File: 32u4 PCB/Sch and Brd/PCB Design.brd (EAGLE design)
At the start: 95.8 x 64.6 mm, 54 parts, among them J1 AVR_SPI_PROG_3X2PTH, J2 AMP FCI 10103594-0001LF, Q1 16MHz, U1 ATMEGA32U4-AU

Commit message: Started routinng
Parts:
- removed JP1: (no value), pinhead:1X02
- removed USB-ASP: AVR_SPI_PROG_5X2PTH2, SparkFun-Connectors:2X5-SHROUDED
- added I2C_OLED: (no value), pinhead:1X04
- added MPU6040: (no value), pinhead:1X08
- added SPI_SD_CARD: (no value), pinhead:1X06
- added X1: (no value), con-ptr500:AK500/2-H
- moved R12 153.5 mm to (75.7, 32.3), turned to 90 degrees
- moved JP5 145.2 mm to (78.2, -1.78), turned to 90 degrees
- moved JP4 143.4 mm to (76.5, 1.78), turned to 90 degrees
- moved JP3 141.7 mm to (84.8, -2.03), turned to 90 degrees
- moved R11 139.7 mm to (73.2, 31.0), turned to 90 degrees
- moved JP2 137.6 mm to (66.0, 30.0), turned to 90 degrees
- moved BUTTON_2 123.7 mm to (54.6, 0.00), turned to 180 degrees
- moved BUTTON_1 108.9 mm to (68.6, -0.25)
- moved POWER_PORT 105.4 mm to (72.6, 17.8), turned to 90 degrees
- moved C11 97.5 mm to (43.2, 31.8), turned to 180 degrees
- moved PB2 80.5 mm to (33.5, 50.3), turned to 90 degrees
- moved CONT 75.4 mm to (82.3, 12.2), turned to 270 degrees
- moved R10 73.1 mm to (23.4, 20.3), turned to 180 degrees
- moved R8 72.8 mm to (28.4, 49.3), turned to 90 degrees
- moved PB1 70.7 mm to (26.9, 52.1), turned to 90 degrees
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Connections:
- net PD2 renamed PD2/RXD1
- net PD3 renamed PD3/TXD1
- net PF4 renamed PF4/TCK
- net PF5 renamed PF5/TMS
- net PF6 renamed PF6/TDO
- net PF7 renamed PF7/TDI
- removed net PB1: J1.3, PORT_B.3, PORT_B.4, U1.9, USB-ASP.7
- removed net PB2: J1.4, PORT_B.5, PORT_B.6, U1.10, USB-ASP.1
- removed net PB3: J1.1, PORT_B.7, PORT_B.8, U1.11, USB-ASP.9
- removed net PD0: PORT_D.1, PORT_D.2, U1.18
- removed net PD1: PORT_D.3, PORT_D.4, U1.19
- new net AD0: MPU6040.7
- new net CS: SPI_SD_CARD.1
- new net INT: MPU6040.8
- new net PB1/SCK: J1.3, PORT_B.3, PORT_B.4, SPI_SD_CARD.2, U1.9
- new net PB2/MOSI: J1.4, PORT_B.5, PORT_B.6, SPI_SD_CARD.3, U1.10
- new net PB3/MISO: J1.1, PORT_B.7, PORT_B.8, SPI_SD_CARD.4, U1.11
- new net PD0/SCL: I2C_OLED.3, MPU6040.3, PORT_D.1, PORT_D.2, U1.18
- new net PD1/SDA: I2C_OLED.4, MPU6040.4, PORT_D.3, PORT_D.4, U1.19
- new net XCL: MPU6040.6
- new net XDA: MPU6040.5
- net +12V: now also X1.2; no longer JP1.1
- net +5V: now also I2C_OLED.2, MPU6040.1, SPI_SD_CARD.5; no longer USB-ASP.2
- net GND: now also I2C_OLED.1, MPU6040.2, SPI_SD_CARD.6, X1.1; no longer JP1.2, USB-ASP.10, USB-ASP.4, USB-ASP.6, USB-ASP.8
- net RESET: no longer USB-ASP.5
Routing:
- net +5V: track 237.2 -> 6.49 mm, vias 6 -> 0
- net RESET: track 113.9 -> 0.00 mm, vias 1 -> 0
- net 3.3V: track 76.8 -> 0.00 mm, vias 2 -> 0
- net PB3/MISO: track 0.00 -> 59.6 mm, vias 0 -> 4
- net PB2: track 56.6 -> 0.00 mm, vias 2 -> 0
- net +12V: track 55.1 -> 0.00 mm, vias 1 -> 0
- net PB2/MOSI: track 0.00 -> 51.6 mm, vias 0 -> 3
- net PB3: track 49.0 -> 0.00 mm
- net PD2/RXD1: track 20.4 -> 68.0 mm, vias 1 -> 3
- net PB1: track 47.5 -> 0.00 mm
- net PD7: track 0.00 -> 44.4 mm, vias 0 -> 2
- net PD6: track 0.00 -> 44.0 mm, vias 0 -> 2
- net PB5: track 2.55 -> 45.0 mm, vias 0 -> 2
- net PD1/SDA: track 0.00 -> 42.3 mm, vias 0 -> 2
- net PB4: track 2.55 -> 44.6 mm, vias 0 -> 2
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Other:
- board text removed: "3.3V"
- board text removed: "5V"
- board text removed: "AREF"
- board text removed: "CTS"
- board text removed: "DTR"
- board text removed: "PB0"
- board text removed: "PB1"
- board text removed: "PB2"
- board text removed: "PB3"
- board text removed: "PB4"
- board text removed: "PB5"
- board text removed: "PC0"
- board text removed: "PC1"
- board text removed: "PC2"
- board text removed: "PC3"
- board text removed: "PC4"
- board text removed: "PC5"
- board text removed: "PD0"
- board text removed: "PD1"
- board text removed: "PD2"
- board text removed: "PD3"
- board text removed: "PD4"
- board text removed: "PD5"
- board text removed: "PD6"
- board text removed: "PD7"
- board text removed: "RESET"
- board text removed: "RX"
- board text removed: "SCL"
- board text removed: "SDA"
- board text removed: "TX"

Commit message: Started routinng
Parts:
- removed CONT: 50k, pot:S64W
- added I2C: (no value), pinhead:1X04
- added R13: 220, resistor:M0805
- moved J1 70.6 mm to (64.8, 58.9), turned to 180 degrees
- moved C4 61.4 mm to (23.9, 58.7)
- moved R11 58.4 mm to (23.6, 0.00)
- moved R12 57.8 mm to (27.9, -0.25)
- moved JP2 55.7 mm to (18.8, 0.51)
- moved C3 51.4 mm to (43.2, 0.25), turned to 270 degrees
- moved BUTTON_1 45.4 mm to (24.4, 10.2)
- moved JP3 45.3 mm to (39.6, 0.00), turned to 270 degrees
- moved JP4 44.7 mm to (31.8, 0.00)
- moved JP5 42.7 mm to (35.6, 0.00), turned to 270 degrees
- moved BUTTON_2 42.1 mm to (13.7, 10.2), turned to 0 degrees
- moved PB1 38.3 mm to (15.5, 15.5), turned to 0 degrees
- moved PB2 35.9 mm to (24.6, 15.5), turned to 0 degrees
- moved R6 34.0 mm to (17.3, 17.5), turned to 180 degrees
- moved R8 31.8 mm to (26.4, 17.5), turned to 180 degrees
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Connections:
- net +12V: no longer X1.2
- net +5V: now also I2C.2; no longer CONT.E
- net GND: now also I2C.1, R13.1; no longer CONT.A, X1.1
- net N$6: now also R13.2; no longer CONT.S
- net PD0/SCL: now also I2C.3
- net PD1/SDA: now also I2C.4
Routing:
- net N$15: track 0.00 -> 60.8 mm, vias 0 -> 2
- net N$13: track 0.00 -> 60.7 mm, vias 0 -> 2
- net PD0/SCL: track 37.5 -> 66.2 mm, vias 0 -> 2
- net PD1/SDA: track 42.3 -> 70.2 mm, vias 2 -> 4
- net PB4: track 44.6 -> 20.0 mm, vias 2 -> 1
- net PB5: track 45.0 -> 20.7 mm, vias 2 -> 1
- net PB0: track 40.0 -> 17.0 mm, vias 1 -> 0
- net RESET: track 0.00 -> 22.9 mm
- net PB6: track 2.54 -> 22.5 mm, vias 0 -> 1
- net PB1/SCK: track 41.7 -> 51.2 mm, vias 2 -> 1
- net PB3/MISO: track 59.6 -> 53.7 mm, vias 4 -> 2
- net PB2/MOSI: track 51.6 -> 54.6 mm
- net PC7: track 29.3 -> 30.2 mm
- net PD3/TXD1: track 65.4 -> 64.6 mm
- net PC6: track 29.1 -> 29.7 mm
- added copper zone on layer 16, net +5V
- removed copper zone on layer 16, net GND
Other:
- board text removed: "GND"
- board text removed: "Vin"

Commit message: Rough layout ready
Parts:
- POWER: device pinhead:2X03 -> pinhead:2X04
- moved R13 31.6 mm to (77.2, 9.91)
- moved C11 30.3 mm to (66.0, 51.6), turned to 90 degrees
- moved C10 17.3 mm to (62.5, 28.7), turned to 0 degrees
- moved C2 7.41 mm to (54.6, 27.7)
- moved C4 4.07 mm to (23.6, 62.7), turned to 90 degrees
- moved C9 2.05 mm to (24.1, 42.7)
- moved R10 1.70 mm to (19.8, 23.6)
- moved R9 1.61 mm to (19.8, 21.1)
- moved R3 1.27 mm to (20.6, 62.7)
- moved POWER 0.51 mm to (35.3, 9.14)
- moved R2 0.51 mm to (32.5, 57.7)
- moved C7 0.18 mm to (20.2, 33.8), turned to 0 degrees
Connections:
- net +5V: now also POWER.3, POWER.4
- net AREF: no longer POWER.3, POWER.4
- net GND: now also POWER.7, POWER.8
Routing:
- net RESET: track 22.9 -> 103.5 mm, vias 0 -> 1
- net +5V: track 6.49 -> 60.6 mm, vias 0 -> 4
- net PE6: track 0.00 -> 38.7 mm, vias 0 -> 1
- net PD0/SCL: track 66.2 -> 96.1 mm
- net +12V: track 0.00 -> 26.6 mm
- net PD1/SDA: track 70.2 -> 96.3 mm
- net PB7: track 2.54 -> 26.0 mm, vias 0 -> 2
- net N$16: track 0.00 -> 19.2 mm, vias 0 -> 1
- net AREF: track 0.00 -> 17.3 mm, vias 0 -> 1
- net D-: track 0.00 -> 12.2 mm, vias 0 -> 2
- net D+: track 0.00 -> 12.1 mm, vias 0 -> 2
- net 3V3: track 0.00 -> 10.2 mm
- net N$6: track 0.00 -> 7.09 mm
- net 3.3V: track 0.00 -> 7.08 mm
- net N$14: track 0.00 -> 3.43 mm
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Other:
- board size 95.8 x 64.6 mm -> 78 x 64.6 mm

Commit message: Routing almost done
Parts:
- removed JP2, JP3, JP4, JP5: JUMPER-SMT_3_1-NC_PASTE_SILK, SparkFun-Jumpers:SMT-JUMPER_3_1-NC_PASTE_SILK
- removed PB1, PB2, PB5: Yellow, SparkFun-LED:LED-0603
- added PC6, PE2, PE6: Yellow, SparkFun-LED:LED-0603
- LCD1: value LCD-16X2NOSILK -> LCD-16X2NOHOLES; device SparkFun-Displays:LCD-16X2_NOSILK -> SparkFun-Displays:LCD-16X2_NOHOLESNOSILK
- R4, R5, R6, R8: value 1K -> 330
- moved LCD1 73.5 mm to (47.5, -13.2), turned to 0 degrees
- moved J2 66.5 mm to (74.7, 0.76), turned to 270 degrees
- moved R13 58.7 mm to (19.6, -1.27), turned to 0 degrees
- moved R7 56.2 mm to (50.5, 4.83), turned to 0 degrees
- moved R10 53.4 mm to (67.8, 0.25), turned to 0 degrees
- moved R9 51.4 mm to (67.8, 2.79), turned to 0 degrees
- moved I2C 32.5 mm to (42.2, 66.5), turned to 180 degrees
- moved POW 28.4 mm to (39.4, 15.7), turned to 90 degrees
- moved R6 27.8 mm to (45.0, 20.3)
- moved R4 24.3 mm to (45.0, 24.9)
- moved X1 24.2 mm to (11.7, 51.3)
- moved C3 20.9 mm to (31.8, 17.8), turned to 0 degrees
- moved R5 19.3 mm to (31.8, 20.3)
- moved R8 19.2 mm to (45.0, 22.6)
- moved R12 16.2 mm to (31.8, 15.5), turned to 0 degrees
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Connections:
- removed net CS: SPI_SD_CARD.1
- removed net D4: LCD1.11
- removed net D5: LCD1.12
- removed net D6: LCD1.13
- removed net D7: LCD1.14
- removed net E: LCD1.6
- removed net N$10: PB1.A
- removed net N$11: PB2.A
- removed net N$12: PB5.A
- removed net N$17: JP2.2, R11.1
- removed net N$18: BUTTON_1.3, BUTTON_1.4, JP3.2
- removed net N$19: BUTTON_2.3, BUTTON_2.4, JP5.2
- removed net N$20: JP4.2, R12.1
- removed net PB0: PORT_B.1, PORT_B.2, U1.8
- removed net RS: LCD1.4
- new net PB0/SS: PORT_B.1, PORT_B.2, SPI_SD_CARD.1, U1.8
- net +5V: now also R11.1, R12.1; no longer JP2.1, JP3.3, JP4.1, JP5.3
- net GND: now also BUTTON_1.3, BUTTON_1.4, BUTTON_2.3, BUTTON_2.4; no longer JP2.3, JP3.1, JP4.3, JP5.1
- net N$1: now also PC6.C; no longer PB5.C
- net N$3: now also PE6.C; no longer PB1.C
- net N$7: now also PE2.C; no longer PB2.C
- net PC6: now also PC6.A
- net PD0/SCL: now also I2C.4; no longer I2C.3
- net PD1/SDA: now also I2C.3; no longer I2C.4
- net PE2: now also PE2.A
- net PE6: now also PE6.A
- net PF0: now also LCD1.4
- net PF1: now also LCD1.6
- net PF4/TCK: now also LCD1.11
- net PF5/TMS: now also LCD1.12
- net PF6/TDO: now also LCD1.13
- net PF7/TDI: now also LCD1.14
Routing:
- net PIN: track 0.00 -> 61.1 mm, vias 0 -> 2
- net PF0: track 24.8 -> 80.3 mm
- net PF1: track 24.1 -> 70.0 mm
- net N$13: track 61.6 -> 33.4 mm, vias 2 -> 0
- net PF4/TCK: track 23.3 -> 50.1 mm
- net PF5/TMS: track 22.8 -> 48.9 mm
- net PB2/MOSI: track 54.6 -> 29.3 mm, vias 3 -> 4
- net PB1/SCK: track 51.2 -> 26.6 mm
- net PB0/SS: track 0.00 -> 21.9 mm
- net N$15: track 62.6 -> 41.2 mm
- net PB3/MISO: track 53.7 -> 32.7 mm, vias 2 -> 1
- net PF6/TDO: track 23.5 -> 43.5 mm
- net PF7/TDI: track 24.2 -> 42.8 mm
- net PD3/TXD1: track 64.8 -> 82.6 mm, vias 4 -> 2
- net PB0: track 16.6 -> 0.00 mm
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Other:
- board size 78 x 64.6 mm -> 71.6 x 74.8 mm

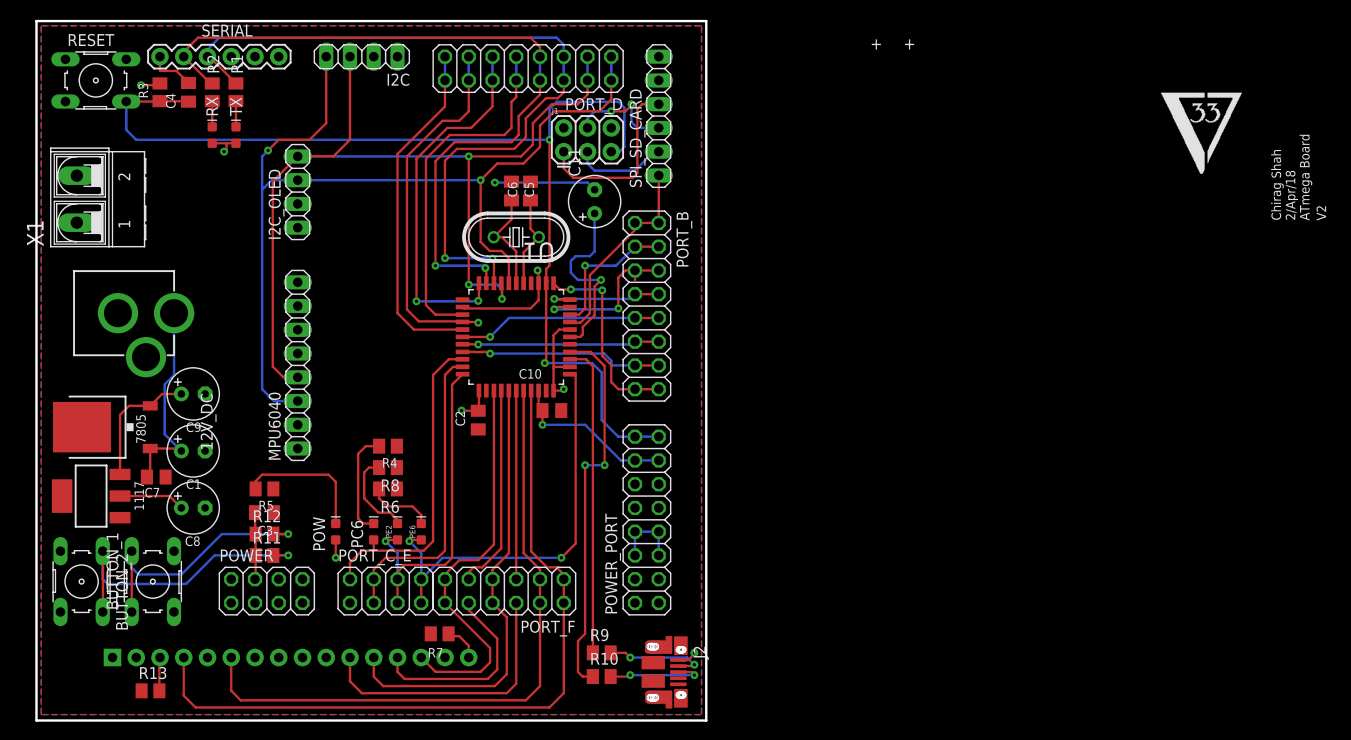
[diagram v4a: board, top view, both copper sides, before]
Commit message: Routing done - Awiiting verification
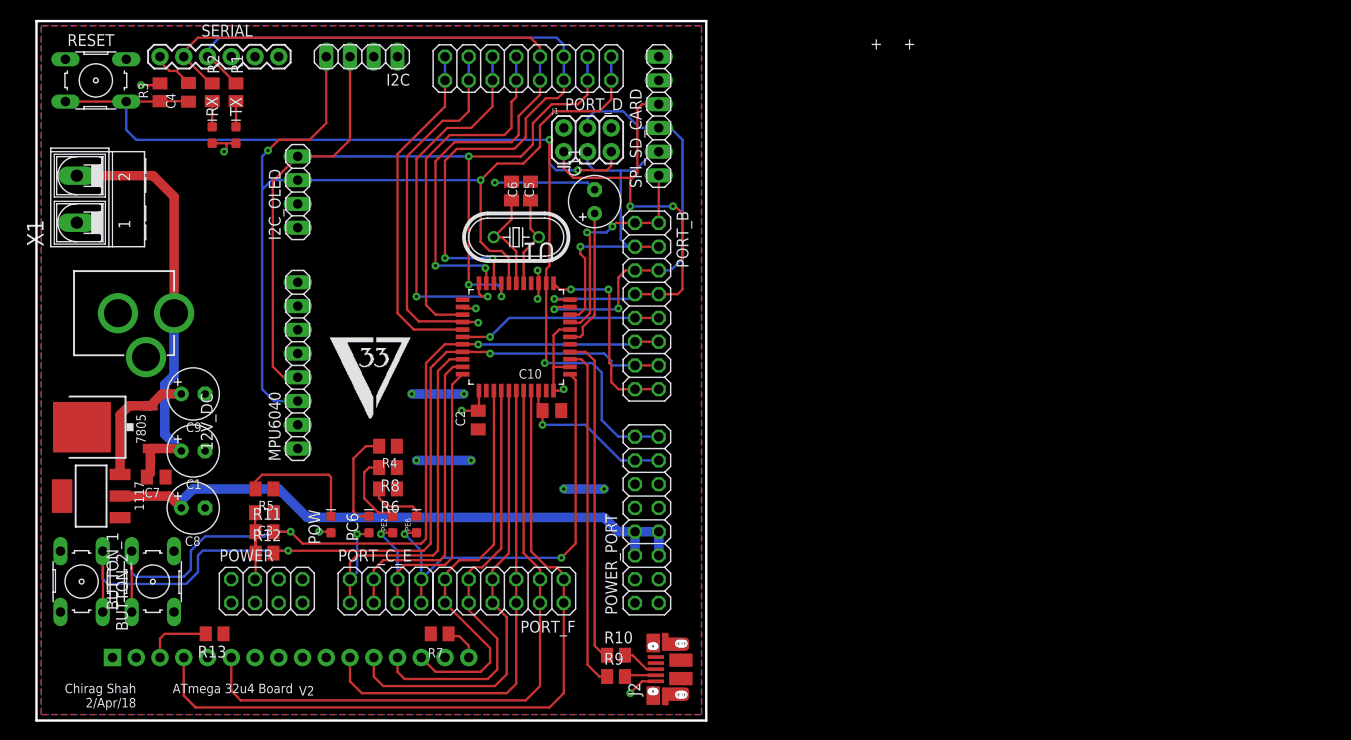
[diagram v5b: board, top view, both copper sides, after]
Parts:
- R13: value 220 -> 4k7
- moved R13 9.18 mm to (26.4, 4.83), turned to 180 degrees
- moved R9 2.96 mm to (69.3, 0.25)
- moved R10 2.75 mm to (69.3, 2.54)
- moved R11 2.54 mm to (31.8, 15.7)
- moved R12 2.03 mm to (31.8, 13.5)
- moved PE6 0.92 mm to (48.0, 16.5)
- moved PC6 0.92 mm to (42.9, 16.5)
- moved PE2 0.92 mm to (45.5, 16.5)
- moved POW 0.92 mm to (38.9, 16.5)
- moved J2 0.36 mm to (74.9, 1.02), turned to 90 degrees
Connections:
- removed net 3.3V: 1117.2, C8.+
- removed net PIN: BUTTON_1.1, BUTTON_1.2, BUTTON_2.1, BUTTON_2.2, R11.2, R12.2
- net +12V: now also X1.2
- net 3V3: now also 1117.2, C8.+
- net GND: now also X1.1
- net PB5: now also BUTTON_1.1, BUTTON_1.2, R11.2
- net PB6: now also BUTTON_2.1, BUTTON_2.2, R12.2
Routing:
- net PB6: track 21.9 -> 94.1 mm, vias 1 -> 2
- net PB5: track 21.1 -> 90.9 mm, vias 1 -> 2
- net PIN: track 61.1 -> 0.00 mm, vias 2 -> 0
- net 3V3: track 7.62 -> 66.4 mm
- net +12V: track 22.5 -> 46.3 mm
- net PB3/MISO: track 32.7 -> 52.7 mm, vias 1 -> 3
- net PB2/MOSI: track 29.3 -> 45.3 mm, vias 4 -> 2
- net GND: track 11.0 -> 26.7 mm, vias 1 -> 7
- net PB1/SCK: track 26.6 -> 36.3 mm
- net PC6: track 35.0 -> 43.1 mm, vias 0 -> 1
- net D-: track 11.3 -> 3.37 mm, vias 2 -> 0
- net 3.3V: track 7.08 -> 0.00 mm
- net D+: track 10.9 -> 3.93 mm, vias 2 -> 0
- net N$15: track 41.2 -> 35.3 mm, vias 2 -> 0
- net N$16: track 20.0 -> 15.0 mm, vias 1 -> 0
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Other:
- board text added: "ATmega 32u4 Board"
- board text removed: "ATmega Board"
